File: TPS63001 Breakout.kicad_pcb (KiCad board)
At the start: 2 copper layers, 20.5 x 20 mm, 15 parts, among them P1 CONN_01X01, P2 CONN_01X01, P3 CONN_01X05, U1 TPS63001

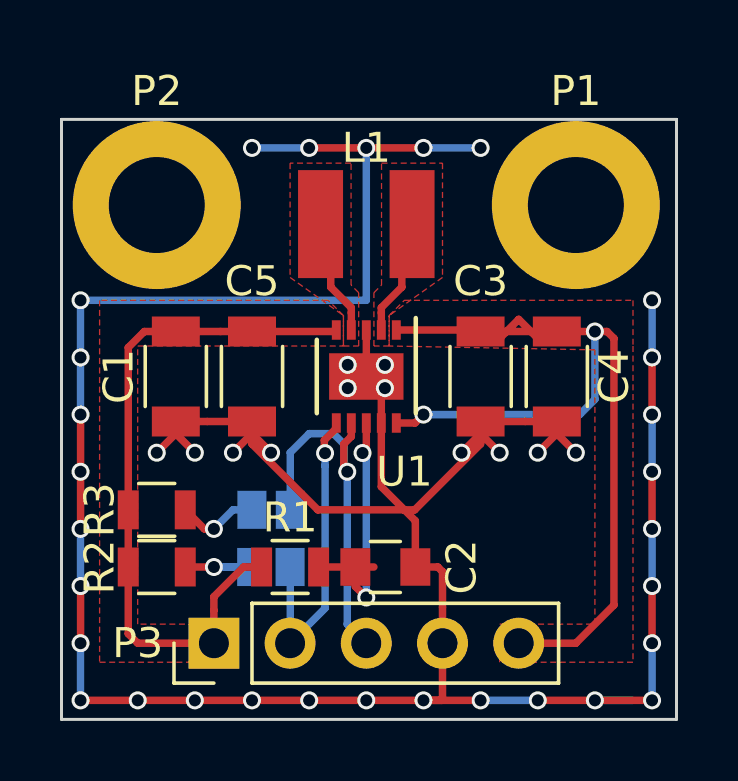
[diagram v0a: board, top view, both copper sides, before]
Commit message: change pullups for PS/SYNC and EN to VCCA filtered supply
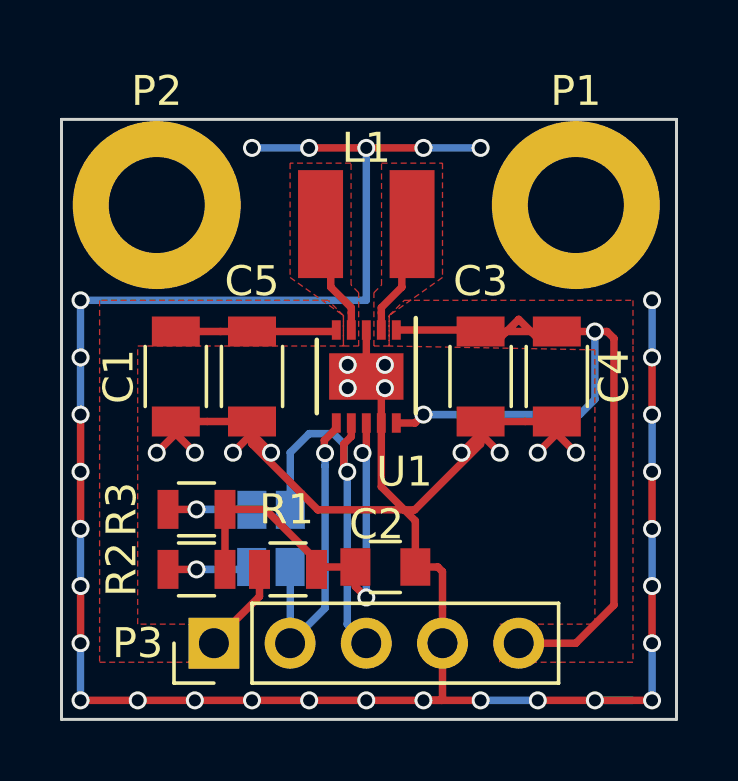
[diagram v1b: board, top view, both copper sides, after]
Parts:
- moved R2 1.33 mm to (120.5, 94.0), turned to 180 degrees
- moved R3 1.33 mm to (120.5, 92.0), turned to 180 degrees
- moved R1 0.11 mm to (123.5, 94.0)
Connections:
- R2 pad 1: VCC -> Net-(C2-Pad1)
- R3 pad 1: VCC -> Net-(C2-Pad1)
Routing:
- net VCC: track 23.3 -> 8.46 mm
- net Net-(C2-Pad1): track 8.93 -> 14.4 mm
- net Net-(JP1-Pad1): track 3.48 -> 2.82 mm
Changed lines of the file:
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@@
   (general
     (links 31)
-    (no_connects 2)
+    (no_connects 0)
     (area 115.949999 78.949999 136.550001 99.050001)
     (thickness 1.6)
     (drawings 8)
-    (tracks 202)
+    (tracks 196)
     (zones 0)
     (modules 15)
@@
       (padsonsilk false)
       (subtractmaskfromsilk false)
-      (outputformat 1)
+      (outputformat 4)
       (mirror false)
       (drillshape 0)
@@
     (tags "capacitor 0805")
     (attr smd)
-    (fp_text reference C2 (at 2.54 0 90) (layer F.SilkS)
+    (fp_text reference C2 (at -0.295 -1.42 180) (layer F.SilkS)
       (effects (font (size 1 1) (thickness 0.15)))
     )
@@
   )
   (module Resistors_SMD:R_0805 (layer F.Cu)
-    (at 123.62 93.92)
+    (at 123.55 94)
     (descr "Resistor SMD 0805, reflow soldering, Vishay (see dcrcw.pdf)")
     (tags "resistor 0805")
     (attr smd)
-    (fp_text reference R1 (at 0 -1.65) (layer F.SilkS)
+    (fp_text reference R1 (at -0.05 -2) (layer F.SilkS)
       (effects (font (size 1 1) (thickness 0.15)))
     )
@@
   )
   (module Resistors_SMD:R_0805 (layer F.Cu)
-    (at 119.175 93.92)
+    (at 120.5 94 180)
     (descr "Resistor SMD 0805, reflow soldering, Vishay (see dcrcw.pdf)")
     (tags "resistor 0805")
     (attr smd)
-    (fp_text reference R2 (at -1.905 0 90) (layer F.SilkS)
-      (effects (font (size 1 1) (thickness 0.15)))
-    )
-    (fp_text value 4K7 (at 0 1.75) (layer F.Fab)
-      (effects (font (size 1 1) (thickness 0.15)))
-    )
-    (fp_text user %R (at 0 -1.65) (layer F.Fab)
+    (fp_text reference R2 (at 2.5 0 270) (layer F.SilkS)
+      (effects (font (size 1 1) (thickness 0.15)))
+    )
+    (fp_text value 4K7 (at 0 1.75 180) (layer F.Fab)
+      (effects (font (size 1 1) (thickness 0.15)))
+    )
+    (fp_text user %R (at 0 -1.65 180) (layer F.Fab)
       (effects (font (size 1 1) (thickness 0.15)))
     )
@@
     (fp_line (start 1.55 0.9) (end 1.55 -0.9) (layer F.CrtYd) (width 0.05))
     (fp_line (start 1.55 0.9) (end -1.55 0.9) (layer F.CrtYd) (width 0.05))
-    (pad 1 smd rect (at -0.95 0) (size 0.7 1.3) (layers F.Cu F.Paste F.Mask)
-      (net 1 VCC))
-    (pad 2 smd rect (at 0.95 0) (size 0.7 1.3) (layers F.Cu F.Paste F.Mask)
+    (pad 1 smd rect (at -0.95 0 180) (size 0.7 1.3) (layers F.Cu F.Paste F.Mask)
+      (net 3 "Net-(C2-Pad1)"))
+    (pad 2 smd rect (at 0.95 0 180) (size 0.7 1.3) (layers F.Cu F.Paste F.Mask)
       (net 11 "Net-(JP1-Pad1)"))
     (model Resistors_SMD.3dshapes/R_0805.wrl
@@
   )
   (module Resistors_SMD:R_0805 (layer F.Cu)
-    (at 119.175 92.015)
+    (at 120.5 92 180)
     (descr "Resistor SMD 0805, reflow soldering, Vishay (see dcrcw.pdf)")
     (tags "resistor 0805")
     (attr smd)
-    (fp_text reference R3 (at -1.905 0 90) (layer F.SilkS)
-      (effects (font (size 1 1) (thickness 0.15)))
-    )
-    (fp_text value 4K7 (at 0 1.75) (layer F.Fab)
-      (effects (font (size 1 1) (thickness 0.15)))
-    )
-    (fp_text user %R (at 0 -1.65) (layer F.Fab)
+    (fp_text reference R3 (at 2.5 0 270) (layer F.SilkS)
+      (effects (font (size 1 1) (thickness 0.15)))
+    )
+    (fp_text value 4K7 (at 0 1.75 180) (layer F.Fab)
+      (effects (font (size 1 1) (thickness 0.15)))
+    )
+    (fp_text user %R (at 0 -1.65 180) (layer F.Fab)
       (effects (font (size 1 1) (thickness 0.15)))
     )
@@
     (fp_line (start 1.55 0.9) (end 1.55 -0.9) (layer F.CrtYd) (width 0.05))
     (fp_line (start 1.55 0.9) (end -1.55 0.9) (layer F.CrtYd) (width 0.05))
-    (pad 1 smd rect (at -0.95 0) (size 0.7 1.3) (layers F.Cu F.Paste F.Mask)
-      (net 1 VCC))
-    (pad 2 smd rect (at 0.95 0) (size 0.7 1.3) (layers F.Cu F.Paste F.Mask)
+    (pad 1 smd rect (at -0.95 0 180) (size 0.7 1.3) (layers F.Cu F.Paste F.Mask)
+      (net 3 "Net-(C2-Pad1)"))
+    (pad 2 smd rect (at 0.95 0 180) (size 0.7 1.3) (layers F.Cu F.Paste F.Mask)
       (net 12 "Net-(JP2-Pad1)"))
     (model Resistors_SMD.3dshapes/R_0805.wrl
@@
       (net 8 "Net-(L1-Pad2)"))
     (model "/Users/florian/Documents/kicad libraries/3d/srn4026.wrl"
-      (at (xyz 0 0 0))
+      (at (xyz 0.0785 0.0785 0.08500000000000001))
       (scale (xyz 0.3937 0.3937 0.3937))
-      (rotate (xyz 0 0 0))
+      (rotate (xyz 90 0 0))
     )
   )
@@
   (gr_line (start 136.5 99) (end 136.5 79) (angle 90) (layer Edge.Cuts) (width 0.1))
   (gr_line (start 116 99) (end 136.5 99) (angle 90) (layer Edge.Cuts) (width 0.1))
+  (segment (start 122.6 94) (end 122.6 94.9) (width 0.25) (layer F.Cu) (net 1))
+  (segment (start 122.6 94.9) (end 121.08 96.42) (width 0.25) (layer F.Cu) (net 1))
+  (segment (start 121.08 96.42) (end 121.08 96.46) (width 0.25) (layer F.Cu) (net 1))
   (segment (start 122.35 86.07) (end 125.11 86.07) (width 0.25) (layer F.Cu) (net 1))
   (segment (start 125.11 86.07) (end 125.16 86.02) (width 0.25) (layer F.Cu) (net 1))
   (segment (start 122.35 86.07) (end 121.3 86.07) (width 0.25) (layer F.Cu) (net 1))
   (segment (start 121.3 86.07) (end 119.81 86.07) (width 0.25) (layer F.Cu) (net 1))
-  (segment (start 118.225 92.015) (end 118.225 86.605) (width 0.25) (layer F.Cu) (net 1))
-  (segment (start 118.225 86.605) (end 118.76 86.07) (width 0.25) (layer F.Cu) (net 1))
-  (segment (start 118.76 86.07) (end 119.81 86.07) (width 0.25) (layer F.Cu) (net 1))
-  (segment (start 118.225 92.015) (end 118.225 93.92) (width 0.25) (layer F.Cu) (net 1))
-  (segment (start 121.08 96.46) (end 118.54 96.46) (width 0.25) (layer F.Cu) (net 1))
-  (segment (start 118.54 96.46) (end 118.225 96.145) (width 0.25) (layer F.Cu) (net 1))
-  (segment (start 118.225 96.145) (end 118.225 93.92) (width 0.25) (layer F.Cu) (net 1))
-  (segment (start 122.67 93.92) (end 122.07 93.92) (width 0.25) (layer F.Cu) (net 1))
-  (segment (start 122.07 93.92) (end 121.08 94.91) (width 0.25) (layer F.Cu) (net 1))
-  (segment (start 121.08 94.91) (end 121.08 95.36) (width 0.25) (layer F.Cu) (net 1))
-  (segment (start 121.08 95.36) (end 121.08 96.46) (width 0.25) (layer F.Cu) (net 1))
   (segment (start 135.685 86.935) (end 135.685 85.03) (width 0.25) (layer B.Cu) (net 2))
   (via (at 135.685 85.03) (size 0.6) (drill 0.4) (layers F.Cu B.Cu) (net 2))
@@
   (segment (start 128.7 94.075) (end 128.7 95.257919) (width 0.25) (layer F.Cu) (net 2))
   (segment (start 128.7 95.257919) (end 128.7 96.46) (width 0.25) (layer F.Cu) (net 2))
+  (segment (start 121.45 92) (end 122.8 92) (width 0.25) (layer F.Cu) (net 3))
+  (segment (start 122.8 92) (end 124.5 93.7) (width 0.25) (layer F.Cu) (net 3))
+  (segment (start 124.5 93.7) (end 124.5 94) (width 0.25) (layer F.Cu) (net 3))
+  (segment (start 121.45 94) (end 121.45 92) (width 0.25) (layer F.Cu) (net 3))
   (segment (start 126.16 94.936) (end 126.16 90.245334) (width 0.25) (layer B.Cu) (net 3))
   (segment (start 126.16 90.245334) (end 126.03499 90.120324) (width 0.25) (layer B.Cu) (net 3))
@@
   (segment (start 125.795 94.571) (end 126.16 94.936) (width 0.25) (layer F.Cu) (net 3))
   (via (at 126.16 94.936) (size 0.6) (drill 0.4) (layers F.Cu B.Cu) (net 3))
-  (segment (start 125.795 93.92) (end 126.414 93.92) (width 0.25) (layer F.Cu) (net 3))
   (segment (start 126.16 89.12) (end 126.16 89.995314) (width 0.25) (layer F.Cu) (net 3))
   (segment (start 126.16 89.995314) (end 126.03499 90.120324) (width 0.25) (layer F.Cu) (net 3))
@@
   (segment (start 125.66 85.275) (end 125.66 85.445) (width 0.25) (layer F.Cu) (net 8))
   (segment (start 125.66 86.02) (end 125.66 85.445) (width 0.25) (layer F.Cu) (net 8))
-  (segment (start 121.08 93.92) (end 122.34 93.92) (width 0.25) (layer B.Cu) (net 11))
-  (segment (start 122.345 93.92) (end 121.08 93.92) (width 0.25) (layer B.Cu) (net 11))
-  (segment (start 121.08 93.92) (end 120.125 93.92) (width 0.25) (layer F.Cu) (net 11))
-  (via (at 121.08 93.92) (size 0.6) (drill 0.4) (layers F.Cu B.Cu) (net 11))
-  (segment (start 121.08 92.65) (end 121.715 92.015) (width 0.25) (layer B.Cu) (net 12))
-  (via (at 121.08 92.65) (size 0.6) (drill 0.4) (layers F.Cu B.Cu) (net 12))
-  (segment (start 120.76 92.65) (end 120.125 92.015) (width 0.25) (layer F.Cu) (net 12))
-  (segment (start 121.08 92.65) (end 120.76 92.65) (width 0.25) (layer F.Cu) (net 12))
-  (segment (start 122.345 92.015) (end 121.715 92.015) (width 0.25) (layer B.Cu) (net 12))
+  (segment (start 120.5 94) (end 122.26 94) (width 0.25) (layer B.Cu) (net 11))
+  (segment (start 122.26 94) (end 122.34 93.92) (width 0.25) (layer B.Cu) (net 11))
+  (segment (start 119.55 94) (end 120.5 94) (width 0.25) (layer F.Cu) (net 11))
+  (via (at 120.5 94) (size 0.6) (drill 0.4) (layers F.Cu B.Cu) (net 11))
+  (segment (start 120.5 92) (end 122.33 92) (width 0.25) (layer B.Cu) (net 12))
+  (segment (start 122.33 92) (end 122.345 92.015) (width 0.25) (layer B.Cu) (net 12))
+  (segment (start 119.55 92) (end 120.5 92) (width 0.25) (layer F.Cu) (net 12))
+  (via (at 120.5 92) (size 0.6) (drill 0.4) (layers F.Cu B.Cu) (net 12))
   (zone (net 2) (net_name GND) (layer B.Cu) (hatch edge 0.508)
     (connect_pads yes (clearance 0.254))

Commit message: silkscreen improvements
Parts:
- added REF***: OSHW-Logo2_7.3x6mm_SilkScreen, Symbols:OSHW-Logo2_7.3x6mm_SilkScreen, B.Cu at (119.5, 89.0)
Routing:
- net GND: track 112.6 -> 111.9 mm
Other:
- outline, holes or cut-outs redrawn
- board text added: "+3V3"
- board text added: "Buck-Boost 1,8-5,5V Vin 3,3V Vout 800mA Iout v1 by @kugel2"
- board text added: "GND"
- board text added: "SYNC"
- board text added: "VCC"
- board text removed: "Buck-Boost 1,8-5,5V Vin 3,3V Vout 800mA Iout"
